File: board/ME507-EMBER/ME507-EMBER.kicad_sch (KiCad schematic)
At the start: 6 parts, among them J1 Screw_Terminal_01x02, J2 Screw_Terminal_01x02, J3 Screw_Terminal_01x02, Q1 Q_NMOS_GDS

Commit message: modified:   board/ME507-EMBER/ME507-EMBER.kicad_sch 	deleted:    board/ME507-EMBER/~ME507-EMBER.kicad_sch.lck
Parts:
- removed A1: Adafruit_Feather_HUZZAH32_ESP32, Module:Adafruit_Feather, symbol MCU_Module:Adafruit_Feather_HUZZAH32_ESP32
- removed J1, J3: Screw_Terminal_01x02, symbol Connector:Screw_Terminal_01x02
- removed J2: Screw_Terminal_01x02, TerminalBlock_4Ucon:TerminalBlock_4Ucon_1x02_P3.50mm_Horizontal, symbol Connector:Screw_Terminal_01x02
- added C1, C3: 0.1 uF, symbol Device:C_Small
- added C2, C4: 47 uF, symbol Device:C_Small
- added ESP1: ~, ME507F24:ESP32_NodeMCU_KeeYees, symbol ME507F24:ESP32_Node_KY
- added J1: Screw_Terminal_01x08, TerminalBlock_Phoenix:TerminalBlock_Phoenix_MPT-0,5-8-2.54_1x08_P2.54mm_Horizontal, symbol Connector:Screw_Terminal_01x08
- added J2: Screw_Terminal_01x04, symbol Connector:Screw_Terminal_01x04
- added R1: 100, symbol Device:R_US
- added R2, R3: TBR, symbol Device:R_US
- added U1, U2: DRV8871DDA, Package_SO:Texas_HTSOP-8-1EP_3.9x4.9mm_P1.27mm_EP2.95x4.9mm_Mask2.4x3.1mm_ThermalVias, symbol Driver_Motor:DRV8871DDA
- Q1: footprint (none) -> Package_TO_SOT_SMD:TSOT-23
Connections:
- net GND: now also Q1.3 (S), C1.2, C2.2, C3.2, C4.2, J1.2 (Pin_2), J2.2 (Pin_2), R2.1, R3.1, U1.1 (GND), U1.7 (GND), U1.9 (GND), U2.1 (GND), U2.7 (GND), U2.9 (GND)
- net Vm: now reaches D1.1 (K)
- net Vm: now also C1.1, C2.1, C3.1, C4.1, J1.1 (Pin_1), J1.3 (Pin_3), U1.5 (VM), U2.5 (VM)
- net at D1.2 (A): now also Q1.2 (D), J1.4 (Pin_4)
- net at Q1.1 (G): now also R1.2
- new net: ESP1.33 (GPIO21/SDA), J2.3 (Pin_3)
- new net: ESP1.36 (GPIO22/SCL), J2.4 (Pin_4)
- new net: ESP1.27 (GPIO16/RX2), U1.2 (IN2)
- new net: ESP1.28 (GPIO17/TX2), U1.3 (IN1)
- new net: R3.2, U1.4 (ILIM)
- new net: J1.5 (Pin_5), U1.6 (OUT1)
- new net: J1.6 (Pin_6), U1.8 (OUT2)
- new net: ESP1.29 (GPIO5), R1.1
- new net: ESP1.13 (GPIO12), U2.2 (IN2)
- new net: ESP1.15 (GPIO13), U2.3 (IN1)
- new net: R2.2, U2.4 (ILIM)
- new net: J1.7 (Pin_7), U2.6 (OUT1)
- new net: J1.8 (Pin_8), U2.8 (OUT2)
- new net +3V3: ESP1.1 (3V3), J2.1 (Pin_1)
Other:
- note added: "V+ V- S+ S- M+ M- M+ M-"
- note added: "V_IR (+) V_IR (-) SDA SCL"

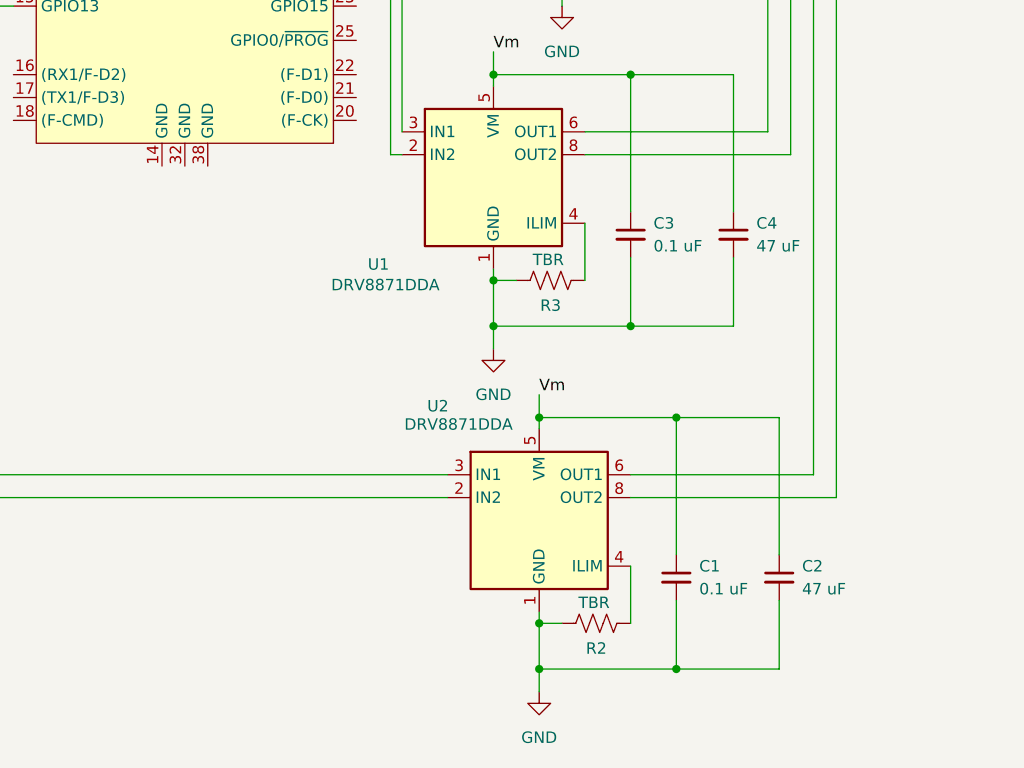
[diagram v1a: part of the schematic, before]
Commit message: modified:   EMBER/src/main.cpp 	new file:   board/ME507-EMBER/ME507-EMBER-backups/ME507-EMBER-2025-10-19_140626.zip 	modified:   board/ME507-EMBER/ME507-EMBER.kicad_sch
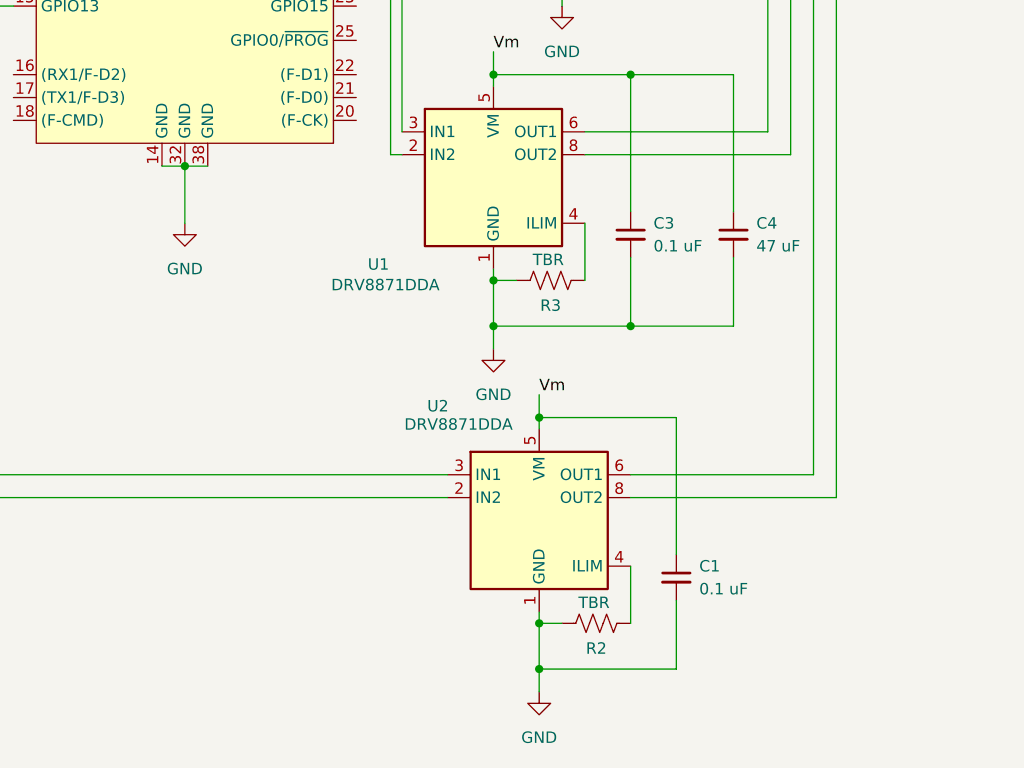
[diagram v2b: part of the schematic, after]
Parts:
- removed C2: 47 uF, symbol Device:C_Small
- Q1: footprint Package_TO_SOT_SMD:TSOT-23 -> Package_TO_SOT_SMD:PQFN_8x8
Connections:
- net GND: now also ESP1.14 (GND), ESP1.32 (GND), ESP1.38 (GND)
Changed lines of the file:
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@@
-	)
-	(junction
-		(at 186.69 162.56)
-		(diameter 0)
-		(color 0 0 0 0)
 	)
 	(junction
@@
 	)
 	(junction
-		(at 186.69 134.62)
+		(at 132.08 106.68)
 		(diameter 0)
 		(color 0 0 0 0)
@@
 	(wire
 		(pts
-			(xy 198.12 134.62) (xy 186.69 134.62)
-		)
-		(stroke
-			(width 0)
-			(type default)
-		)
-	)
-	(wire
-		(pts
 			(xy 176.53 102.87) (xy 196.85 102.87)
 		)
@@
 	(wire
 		(pts
+			(xy 132.08 106.68) (xy 132.08 113.03)
+		)
+		(stroke
+			(width 0)
+			(type default)
+		)
+	)
+	(wire
+		(pts
 			(xy 186.69 162.56) (xy 171.45 162.56)
 		)
@@
 	(wire
 		(pts
-			(xy 198.12 162.56) (xy 186.69 162.56)
-		)
-		(stroke
-			(width 0)
-			(type default)
-		)
-	)
-	(wire
-		(pts
-			(xy 198.12 149.86) (xy 198.12 134.62)
-		)
-		(stroke
-			(width 0)
-			(type default)
-		)
-	)
-	(wire
-		(pts
 			(xy 181.61 143.51) (xy 204.47 143.51)
 		)
@@
 	(wire
 		(pts
-			(xy 198.12 154.94) (xy 198.12 162.56)
-		)
-		(stroke
-			(width 0)
-			(type default)
-		)
-	)
-	(wire
-		(pts
 			(xy 173.99 57.15) (xy 189.23 57.15)
 		)
@@
 	(wire
 		(pts
+			(xy 129.54 106.68) (xy 132.08 106.68)
+		)
+		(stroke
+			(width 0)
+			(type default)
+		)
+	)
+	(wire
+		(pts
 			(xy 171.45 156.21) (xy 171.45 157.48)
 		)
@@
 		(pts
 			(xy 181.61 111.76) (xy 181.61 96.52)
+		)
+		(stroke
+			(width 0)
+			(type default)
+		)
+	)
+	(wire
+		(pts
+			(xy 132.08 106.68) (xy 134.62 106.68)
 		)
 		(stroke
@@
 	(symbol
 		(lib_id "power:GND")
+		(at 132.08 113.03 0)
+		(unit 1)
+		(exclude_from_sim no)
+		(in_bom yes)
+		(on_board yes)
+		(dnp no)
+		(fields_autoplaced yes)
+		(property "Reference" "#PWR08"
+			(at 132.08 119.38 0)
+			(effects
+				(font
+					(size 1.27 1.27)
+				)
+				(hide yes)
+			)
+		)
+		(property "Value" "GND"
+			(at 132.08 118.11 0)
+			(effects
+				(font
+					(size 1.27 1.27)
+				)
+			)
+		)
+		(property "Footprint" ""
+			(at 132.08 113.03 0)
+			(effects
+				(font
+					(size 1.27 1.27)
+				)
+				(hide yes)
+			)
+		)
+		(property "Datasheet" ""
+			(at 132.08 113.03 0)
+			(effects
+				(font
+					(size 1.27 1.27)
+				)
+				(hide yes)
+			)
+		)
+		(property "Description" "Power symbol creates a global label with name \"GND\" , ground"
+			(at 132.08 113.03 0)
+			(effects
+				(font
+					(size 1.27 1.27)
+				)
+				(hide yes)
+			)
+		)
+		(pin "1"
+		)
+		(instances
+			(project "ME507-EMBER"
+				(path "/259d0011-820b-41ae-9d34-b870aa68bb26"
+					(reference "#PWR08")
+					(unit 1)
+				)
+			)
+		)
+	)
+	(symbol
+		(lib_id "power:GND")
 		(at 80.01 49.53 0)
 		(unit 1)
@@
 			)
 		)
-		(property "Footprint" "Package_TO_SOT_SMD:TSOT-23"
+		(property "Footprint" "Package_TO_SOT_SMD:PQFN_8x8"
 			(at 176.53 78.74 0)
 			(effects
@@
 					(unit 1)
 				)
-			)
-		)
-	)
-	(symbol
-		(lib_id "Device:C_Small")
-		(at 198.12 152.4 0)
-		(unit 1)
-		(exclude_from_sim no)
-		(in_bom yes)
-		(on_board yes)
-		(dnp no)
-		(fields_autoplaced yes)
-		(property "Reference" "C2"
-			(at 200.66 151.1362 0)
-			(effects
-				(font
-					(size 1.27 1.27)
-				)
-				(justify left)
-			)
-		)
-		(property "Value" "47 uF"
-			(at 200.66 153.6762 0)
-			(effects
-				(font
-					(size 1.27 1.27)
-				)
-				(justify left)
-			)
-		)
-		(property "Footprint" ""
-			(at 198.12 152.4 0)
-			(effects
-				(font
-					(size 1.27 1.27)
-				)
-				(hide yes)
-			)
-		)
-		(property "Datasheet" "~"
-			(at 198.12 152.4 0)
-			(effects
-				(font
-					(size 1.27 1.27)
-				)
-				(hide yes)
-			)
-		)
-		(property "Description" "Unpolarized capacitor, small symbol"
-			(at 198.12 152.4 0)
-			(effects
-				(font
-					(size 1.27 1.27)
-				)
-				(hide yes)
-			)
-		)
-		(pin "1"
-		)
-		(pin "2"
-		)
-		(instances
-			(project "ME507-EMBER"
-				(path "/259d0011-820b-41ae-9d34-b870aa68bb26"
-					(reference "C2")
-					(unit 1)
-				)

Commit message: new file:   board/ME507-EMBER/ME507-EMBER-backups/ME507-EMBER-2025-10-23_172612.zip 	modified:   board/ME507-EMBER/ME507-EMBER.kicad_pcb 	modified:   board/ME507-EMBER/ME507-EMBER.kicad_prl 	modified:   board/ME507-EMBER/ME507-EMBER.kicad_pro 	modified:   board/ME507-EMBER/ME507-EMBER.kicad_sch 	new file:   board/ME507-EMBER/fp-info-cache
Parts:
- removed J1: Screw_Terminal_01x08, TerminalBlock_Phoenix:TerminalBlock_Phoenix_MPT-0,5-8-2.54_1x08_P2.54mm_Horizontal, symbol Connector:Screw_Terminal_01x08
- added 4.7k1, 4.7k2, 4.7k4: ~, Resistor_SMD:R_1206_3216Metric_Pad1.30x1.75mm_HandSolder, symbol Device:R_US
- added 4.7k3: 4.7k, Resistor_SMD:R_1206_3216Metric_Pad1.30x1.75mm_HandSolder, symbol Device:R_US
- added J1, J3: Screw_Terminal_01x02, TerminalBlock_Phoenix:TerminalBlock_Phoenix_MPT-0,5-2-2.54_1x02_P2.54mm_Horizontal, symbol Connector:Screw_Terminal_01x02
- added J4: Screw_Terminal_01x04, TerminalBlock_Phoenix:TerminalBlock_Phoenix_MPT-0,5-4-2.54_1x04_P2.54mm_Horizontal, symbol Connector:Screw_Terminal_01x04
- added J5: Screw_Terminal_01x08, TerminalBlock_Phoenix:TerminalBlock_Phoenix_MPT-0,5-8-2.54_1x08_P2.54mm_Horizontal, symbol Connector:Screw_Terminal_01x08
- C1, C3: footprint (none) -> Capacitor_SMD:C_0201_0603Metric_Pad0.64x0.40mm_HandSolder
- C4: footprint (none) -> Capacitor_SMD:C_1206_3216Metric_Pad1.33x1.80mm_HandSolder
- J2: footprint (none) -> TerminalBlock_Phoenix:TerminalBlock_Phoenix_MPT-0,5-4-2.54_1x04_P2.54mm_Horizontal
- Q1: value Q_NMOS_GDS -> Q_NMOS_DGS; footprint Package_TO_SOT_SMD:PQFN_8x8 -> Package_TO_SOT_SMD:Vishay_PowerPAK_SC70-6L_Single
- R1: footprint (none) -> Resistor_SMD:R_1206_3216Metric_Pad1.30x1.75mm_HandSolder
- R2, R3: value TBR -> 32k; footprint (none) -> Resistor_SMD:R_1206_3216Metric_Pad1.30x1.75mm_HandSolder
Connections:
- net +3V3: now also 4.7k1.2, 4.7k2.2, 4.7k3.2, 4.7k4.2, J5.1 (Pin_1), J5.5 (Pin_5)
- net GND: now also J3.2 (Pin_2), J5.2 (Pin_2), J5.6 (Pin_6)
- net Vm: now also J1.1 (Pin_1), J3.1 (Pin_1)
- net at D1.2 (A), Q1.2 (D): now also J1.2 (Pin_2)
- net at U1.6 (OUT1): now also J4.1 (Pin_1)
- net at U1.8 (OUT2): now also J4.2 (Pin_2)
- net at U2.6 (OUT1): now also J4.3 (Pin_3)
- net at U2.8 (OUT2): now also J4.4 (Pin_4)
- net at ESP1.5 (GPI34/ADC6): now also 4.7k4.1, J5.3 (Pin_3)
- net at ESP1.6 (GPI35/ADC7): now also 4.7k1.1, J5.4 (Pin_4)
- net at ESP1.7 (GPIO32/ADC4): now also 4.7k2.1, J5.7 (Pin_7)
- net at ESP1.8 (GPIO33/ADC5): now also 4.7k3.1, J5.8 (Pin_8)
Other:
- note added: "En1+ En1- A1 B1 En2+ En2- A2 B2"
- note added: "M1+ M1- M2+ M2-"
- note added: "S+ S-"
- note added: "V+ V-"
- note removed: "V+ V- S+ S- M+ M- M+ M-"

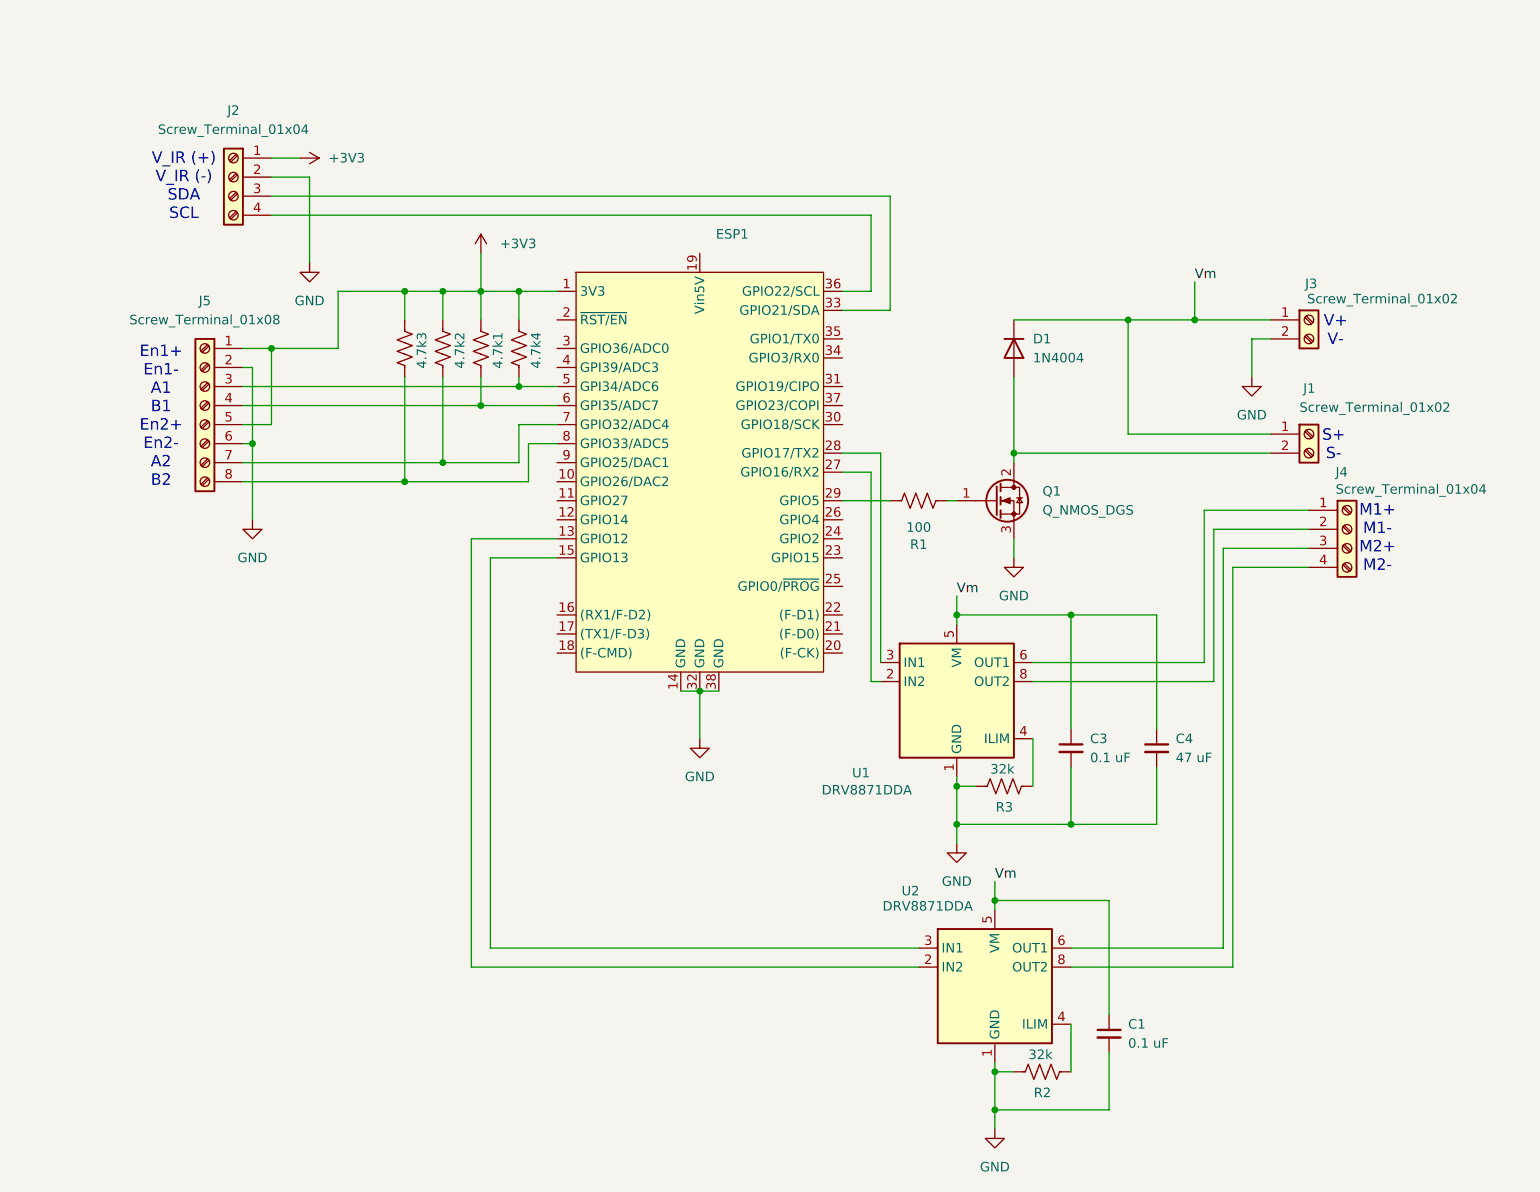
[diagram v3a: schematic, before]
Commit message: new file:   board/ME507-EMBER/EMBER_Footprints.pretty/EMBER_Vishay_PowerPAK_1212-8.kicad_mod 	new file:   board/ME507-EMBER/EMBER_Footprints.pretty/MOSFET_Vishay_PowerPAK_1212-8_Single_JACKSON.kicad_mod 	new file:   board/ME507-EMBER/ME507-EMBER-backups/ME507-EMBER-2025-10-24_173205.zip 	new file:   board/ME507-EMBER/ME507-EMBER-backups/ME507-EMBER-2025-10-24_174214.zip 	new file:   board/ME507-EMBER/ME507-EMBER-backups/ME507-EMBER-2025-10-24_174817.zip 	new file:   board/ME507-EMBER/ME507-EMBER-backups/ME507-EMBER-2025-10-24_175957.zip 	new file:   board/ME507-EMBER/ME507-EMBER-backups/ME507-EMBER-2025-10-24_180838.zip 	modified:   board/ME507-EMBER/ME507-EMBER.kicad_pcb 	modified:   board/ME507-EMBER/ME507-EMBER.kicad_prl 	modified:   board/ME507-EMBER/ME507-EMBER.kicad_pro 	modified:   board/ME507-EMBER/ME507-EMBER.kicad_sch 	modified:   board/ME507-EMBER/fp-info-cache 	new file:   board/ME507-EMBER/fp-lib-table
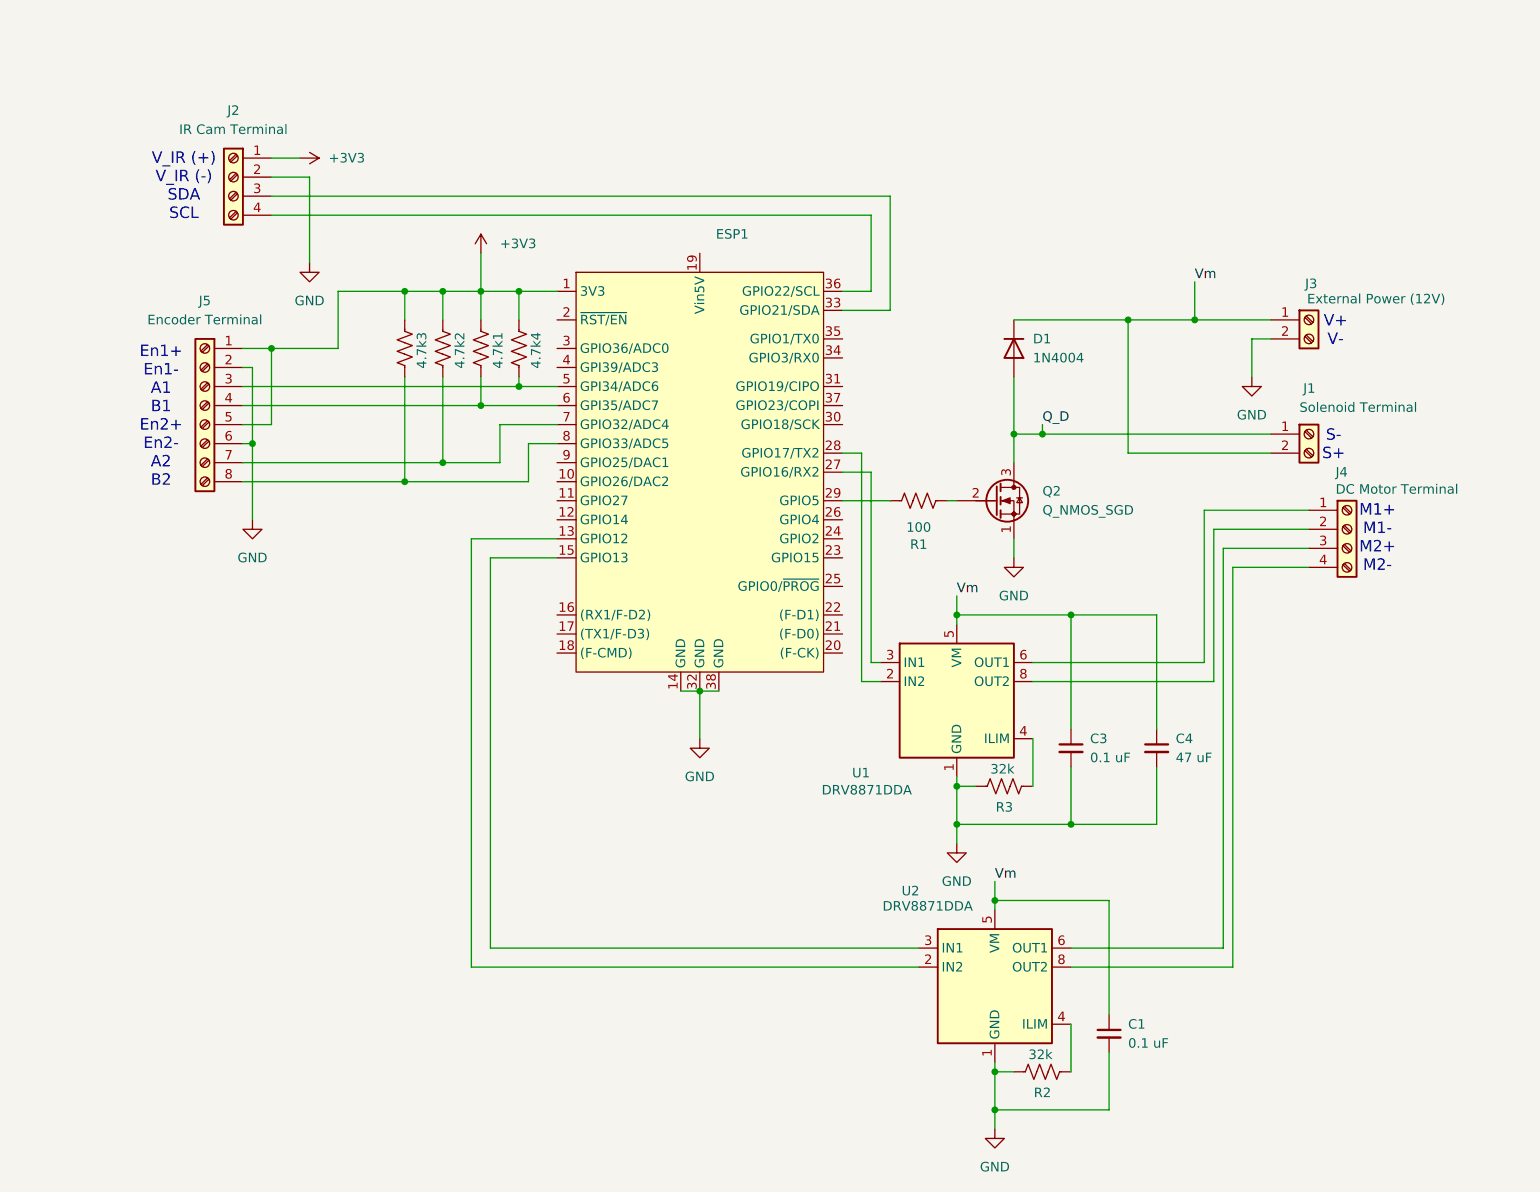
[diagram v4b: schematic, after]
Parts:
- removed Q1: Q_NMOS_DGS, Package_TO_SOT_SMD:Vishay_PowerPAK_SC70-6L_Single, symbol Transistor_FET:Q_NMOS_GDS
- added Q2: Q_NMOS_SGD, EMBER_Footprints:MOSFET_Vishay_PowerPAK_1212-8_Single_JACKSON, symbol Transistor_FET:Q_NMOS_SGD
- C1, C3: footprint Capacitor_SMD:C_0201_0603Metric_Pad0.64x0.40mm_HandSolder -> Capacitor_SMD:C_1206_3216Metric_Pad1.33x1.80mm_HandSolder
- J1: value Screw_Terminal_01x02 -> Solenoid Terminal
- J2: value Screw_Terminal_01x04 -> IR Cam Terminal
- J3: value Screw_Terminal_01x02 -> External Power (12V)
- J4: value Screw_Terminal_01x04 -> DC Motor Terminal
- J5: value Screw_Terminal_01x08 -> Encoder Terminal
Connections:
- net GND: now also Q2.1 (S)
- net Vm: now also J1.2 (Pin_2); no longer J1.1 (Pin_1)
- net at R1.2: now also Q2.2 (G)
- net Q_D: now reaches D1.2 (A)
- net Q_D: now also J1.1 (Pin_1), Q2.3 (D); no longer J1.2 (Pin_2)
- net at U1.2 (IN2): now also ESP1.28 (GPIO17/TX2); no longer ESP1.27 (GPIO16/RX2)
- net at U1.3 (IN1): now also ESP1.27 (GPIO16/RX2); no longer ESP1.28 (GPIO17/TX2)
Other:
- note added: "S- S+"
- note removed: "S+ S-"
